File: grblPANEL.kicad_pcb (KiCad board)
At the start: 4 copper layers, 84 x 55 mm, 147 parts, among them J101 Conn_01x02, J201 2x5x1.27mm, J202 USB_C_Receptacle_USB2.0, J301 Conn_01x02, J401 Conn_01x02, J501 ILI9488, J601 Conn_02x10_Odd_Even, J701 Conn_01x04, J702 Conn_01x04, J703 Conn_01x04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

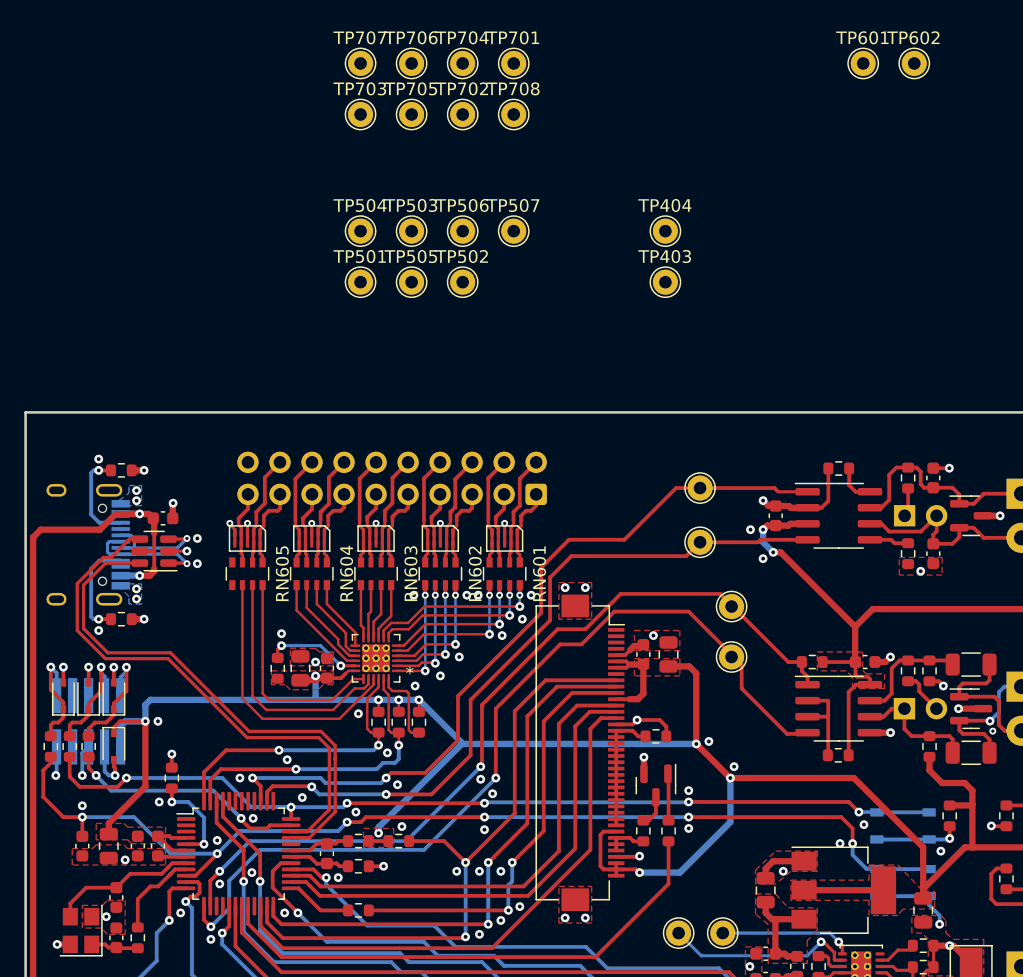
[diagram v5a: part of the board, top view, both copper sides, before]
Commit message: keypad test points
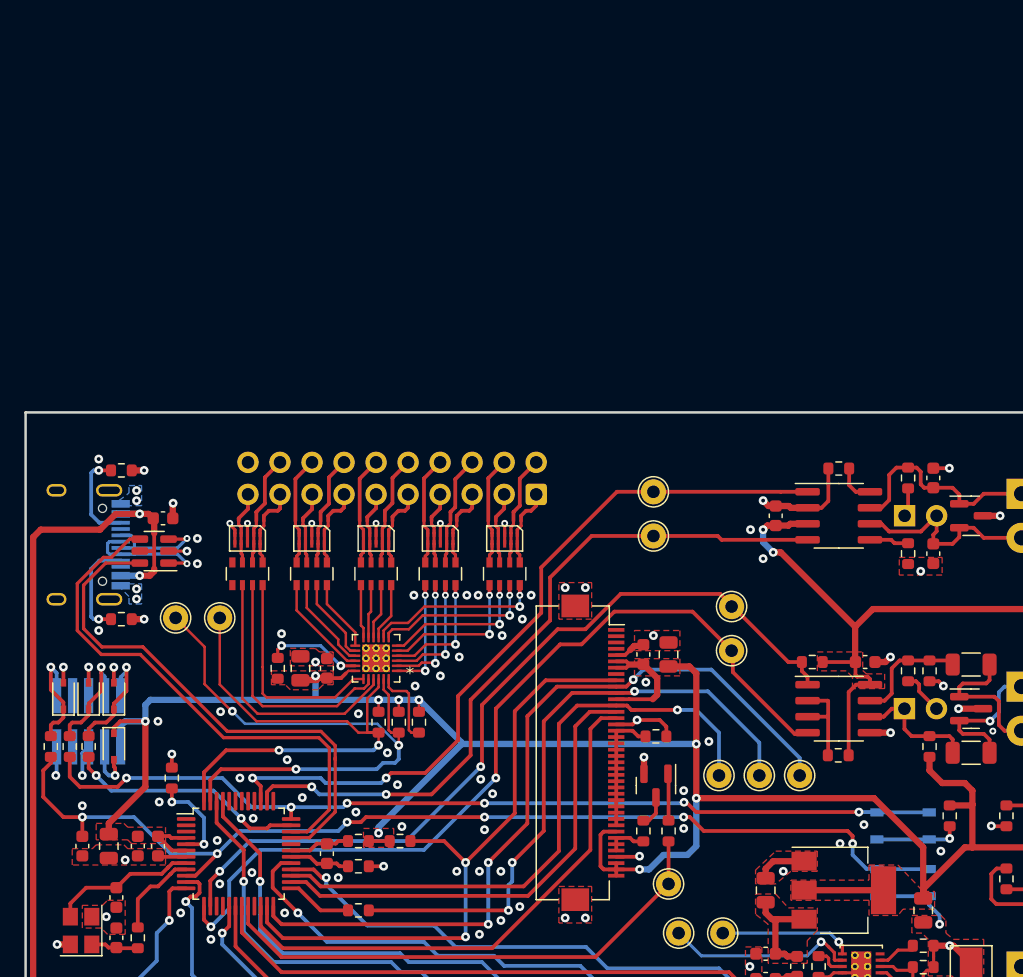
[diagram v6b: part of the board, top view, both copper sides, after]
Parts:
- removed TP403, TP404, TP505, TP506, TP507, TP701, TP702, TP703, TP704, TP705, TP706, TP707, TP708: TestPoint, TestPoint:TestPoint_THTPad_D2.0mm_Drill1.0mm
- R501: value 1k -> 0
- R502: value 10k -> 1k
- R503: value 0 -> 10k
- moved TP602 70.5 mm to (36.4, 145.3)
- moved TP601 70.1 mm to (32.9, 145.3)
- moved TP504 55.5 mm to (82.4, 157.8)
- moved TP501 53.6 mm to (72.0, 166.4)
- moved TP503 49.6 mm to (76.0, 157.8)
- moved TP502 45.7 mm to (79.2, 157.8)
- moved R501 25.4 mm to (47.4, 168.5), turned to 0 degrees
- moved R502 21.4 mm to (72.0, 162.2), turned to 90 degrees
- moved R503 6.41 mm to (50.7, 163.0)
- moved TP302 3.73 mm to (70.8, 138.8)
- moved TP301 3.71 mm to (70.8, 135.3)
- moved TP402 0.50 mm to (77.0, 147.9)
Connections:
- J202 pad S1: unconnected-(J202-PadS1) -> (no net)
- R501 pad 1: DISPLAY_BACKLIGHT -> DISPLAY_SCL
- R501 pad 2: Net-(Q501-Pad1) -> /Display/CONN_SCL
- R502 pad 1: +3V3 -> DISPLAY_BACKLIGHT
- R502 pad 2: DISPLAY_CS -> Net-(Q501-Pad1)
- R503 pad 1: DISPLAY_SCL -> +3V3
- R503 pad 2: /Display/CONN_SCL -> DISPLAY_CS
- TP501 pad 1: DISPLAY_CS -> DISPLAY_BACKLIGHT
- TP502 pad 1: DISPLAY_RESET -> /Display/CONN_SCL
- TP503 pad 1: DISPLAY_BACKLIGHT -> DISPLAY_SDA
- TP504 pad 1: DISPLAY_SCL -> DISPLAY_D/C
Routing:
- net KEYPAD_CLK: track 24.5 -> 48.1 mm, vias 2 -> 3
- net KEYPAD_SDA: track 23.4 -> 43.0 mm
- net DISPLAY_D/C: track 43.9 -> 63.3 mm, vias 2 -> 3
- net /Display/CONN_SCL: track 33.9 -> 49.6 mm, vias 2 -> 3
- net DISPLAY_SDA: track 38.0 -> 50.4 mm, vias 0 -> 1
- net +3V3: track 355.3 -> 356.0 mm
- net GND: vias 117 -> 118

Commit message: stiching vias
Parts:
- moved R501 101.8 mm to (133.8, 114.5)
- moved RN603 99.9 mm to (132.8, 87.8)
- moved TP101 99.9 mm to (160.3, 116.3)
- moved TP102 99.9 mm to (156.8, 116.3)
- moved TP301 99.9 mm to (154.8, 81.3)
- moved TP302 99.9 mm to (154.8, 84.8)
- moved C101 99.9 mm to (172.5, 122.8)
- moved C102 99.9 mm to (170.1, 122.8)
- moved C201 99.9 mm to (111.6, 109.4)
- moved C202 99.9 mm to (113.9, 109.4)
- moved C203 99.9 mm to (115.5, 109.4)
- moved C204 99.9 mm to (128.9, 110.0)
- moved C205 99.9 mm to (109.5, 109.4)
- moved C206 99.9 mm to (112.2, 116.7)
- moved C207 99.9 mm to (112.2, 113.5)
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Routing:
- net /Display/CONN_SCL: track 49.6 -> 46.4 mm
- net DISPLAY_SCL: track 4.65 -> 7.00 mm
- net DISPLAY_SDA: track 50.4 -> 49.3 mm
- net MODBUS_RX: track 65.4 -> 66.2 mm
- net CAN_TX: track 60.0 -> 60.7 mm
- net +3V3: track 356.0 -> 355.4 mm
- net ENCODER_1_A: track 40.4 -> 40.9 mm
- net GND: vias 118 -> 210

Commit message: arrange fab layer text
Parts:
- D301, D401: value CDSOT23-SM712 -> SM712
- Q501: value Q_NPN_BEC - S8050 -> Q_NPN_BEC
